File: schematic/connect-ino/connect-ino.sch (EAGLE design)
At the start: 153 parts

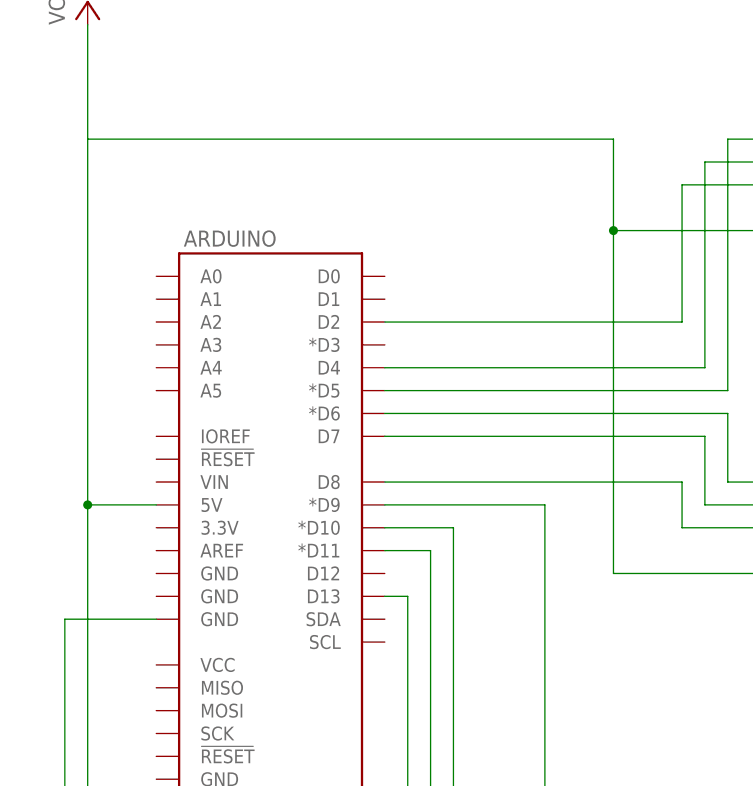
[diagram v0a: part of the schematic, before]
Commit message: Adicionar buzzer
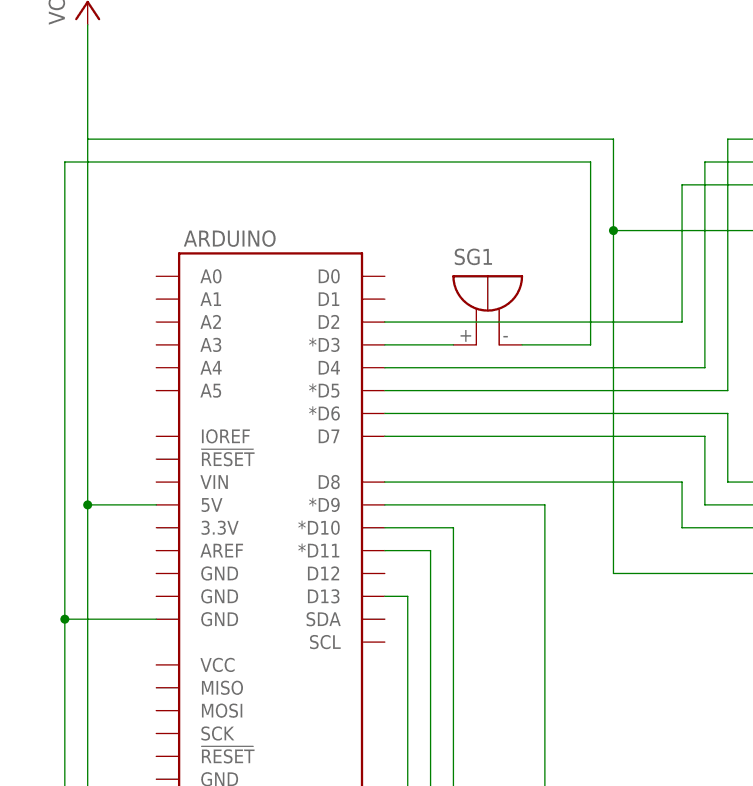
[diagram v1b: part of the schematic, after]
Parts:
- added SG1: F/TMB, buzzer:F/TMB
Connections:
- new net N$39: ARDUINO.*D3, SG1.+
- net GNDA: now also SG1.-
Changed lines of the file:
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@@
 <?xml version="1.0" encoding="utf-8"?>
 <!DOCTYPE eagle SYSTEM "eagle.dtd">
-<eagle version="9.6.0">
+<eagle version="9.6.2">
 <drawing>
 <settings>
@@
 <part name="C7" library="capacitor-wima" library_urn="urn:adsk.eagle:library:116" deviceset="C" device="2,5-3" package3d_urn="urn:adsk.eagle:package:5436/1"/>
 <part name="C8" library="capacitor-wima" library_urn="urn:adsk.eagle:library:116" deviceset="C" device="2,5-3" package3d_urn="urn:adsk.eagle:package:5436/1"/>
+<part name="SG1" library="buzzer" library_urn="urn:adsk.eagle:library:113" deviceset="F/TMB" device="" package3d_urn="urn:adsk.eagle:package:5260/1"/>
 </parts>
 <sheets>
@@
 <attribute name="NAME" x="131.064" y="-40.259" size="1.778" layer="95"/>
 <attribute name="VALUE" x="131.064" y="-45.339" size="1.778" layer="96"/>
+</instance>
+<instance part="SG1" gate="1" x="53.34" y="68.58" smashed="yes">
+<attribute name="NAME" x="50.8" y="74.93" size="1.778" layer="95"/>
 </instance>
 </instances>
@@
 <wire x1="129.54" y1="-45.72" x2="129.54" y2="-48.26" width="0.1524" layer="91"/>
 <junction x="129.54" y="-48.26"/>
+<pinref part="SG1" gate="1" pin="-"/>
+<wire x1="58.42" y1="66.04" x2="66.04" y2="66.04" width="0.1524" layer="91"/>
+<wire x1="66.04" y1="66.04" x2="66.04" y2="86.36" width="0.1524" layer="91"/>
+<wire x1="66.04" y1="86.36" x2="7.62" y2="86.36" width="0.1524" layer="91"/>
+<wire x1="7.62" y1="86.36" x2="7.62" y2="35.56" width="0.1524" layer="91"/>
+<junction x="7.62" y="35.56"/>
 </segment>
 </net>
@@
 </segment>
 </net>
+<net name="N$39" class="0">
+<segment>
+<pinref part="ARDUINO" gate="G$1" pin="*D3"/>
+<pinref part="SG1" gate="1" pin="+"/>
+<wire x1="43.18" y1="66.04" x2="50.8" y2="66.04" width="0.1524" layer="91"/>
+</segment>
+</net>
